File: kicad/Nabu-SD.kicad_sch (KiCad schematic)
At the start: 15 parts, among them J1 Nabu Expansion Slot, J2 ICSP, J3 SD Card, J4 Serial, J5 I2C, J6 OUT1, U1 PIC18F47Q84-E/P, U2 DS1307N+, Y1 32KHz

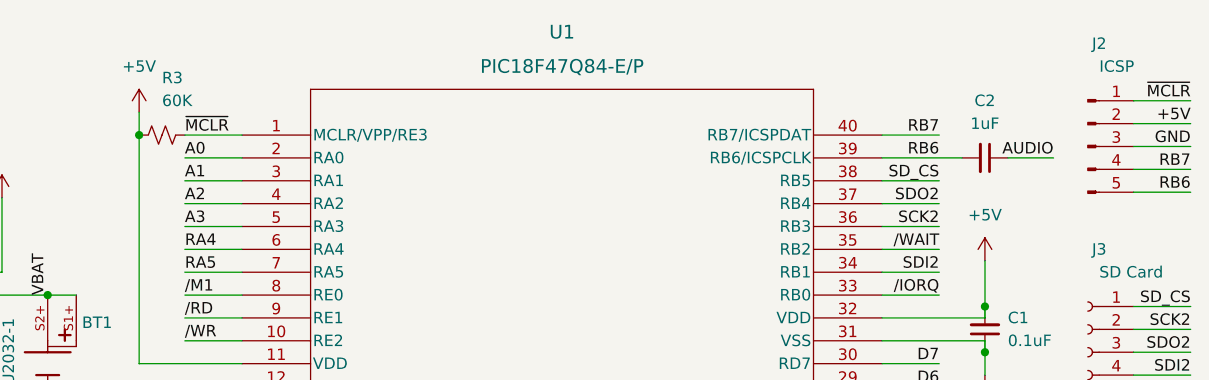
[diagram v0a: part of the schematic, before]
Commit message: Corrected 1 resistor value; Added a Solder Jumper to close AFTER flashing PIC. Reduced the size of the board.  Moved to mostly SMD parts (where possible).
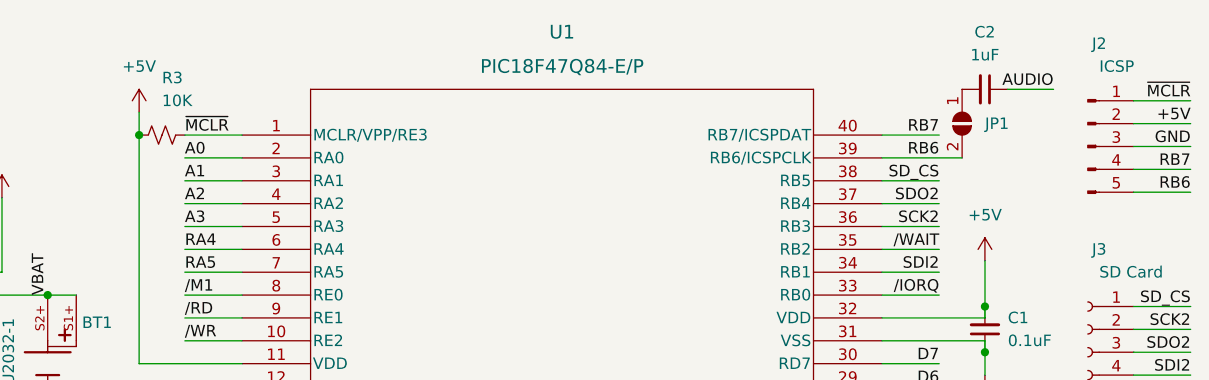
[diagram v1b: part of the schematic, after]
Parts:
- added JP1: ICSP Close, SolderJumper-2_P1.3mm_Open_TrianglePad1.0x1.5mm, symbol Jumper:SolderJumper_2_Open
- R3: value 60K -> 10K; Digi-Key_PN P60.4KCCT-ND -> P10.0KCCT-ND; LCSC C2077261 -> C169253; MPN ERJ-6ENF6042V -> ERJ-6ENF1002V
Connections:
- net RB6: now also JP1.2 (B); no longer C2.2
- new net: C2.2, JP1.1 (A)
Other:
- moved on the sheet: C2
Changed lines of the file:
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@@
+    (stroke (width 0) (type default) (color 0 0 0 0))
+  )
+  (wire (pts (xy 161.29 27.94) (xy 170.18 27.94))
     (stroke (width 0) (type default) (color 0 0 0 0))
   )
@@
     (stroke (width 0) (type default) (color 0 0 0 0))
   )
-  (wire (pts (xy 175.26 27.94) (xy 180.34 27.94))
+  (wire (pts (xy 175.26 20.32) (xy 180.34 20.32))
     (stroke (width 0) (type default) (color 0 0 0 0))
   )
@@
     (stroke (width 0) (type default) (color 0 0 0 0))
   )
-  (wire (pts (xy 161.29 27.94) (xy 170.18 27.94))
-    (stroke (width 0) (type default) (color 0 0 0 0))
-  )
   (wire (pts (xy 161.29 73.66) (xy 167.64 73.66))
     (stroke (width 0) (type default) (color 0 0 0 0))
@@
     (effects (font (size 1.27 1.27)) (justify right bottom))
   )
-  (label "AUDIO" (at 180.34 27.94 180)
+  (label "AUDIO" (at 180.34 20.32 180)
     (effects (font (size 1.27 1.27)) (justify right bottom))
   )
@@
       (effects (font (size 1.27 1.27)) (justify right))
     )
-    (property "Value" "60K" (id 1) (at 81.28 21.59 90)
+    (property "Value" "10K" (id 1) (at 81.28 21.59 90)
       (effects (font (size 1.27 1.27)) (justify right))
     )
@@
       (effects (font (size 1.27 1.27)) hide)
     )
-    (property "Description" "RES SMD 60.4K OHM 1% 1/8W 0805" (id 4) (at 81.28 25.4 0)
-      (effects (font (size 1.27 1.27)) hide)
-    )
-    (property "Digi-Key_PN" "P60.4KCCT-ND" (id 5) (at 81.28 25.4 0)
-      (effects (font (size 1.27 1.27)) hide)
-    )
-    (property "MPN" "ERJ-6ENF6042V" (id 6) (at 81.28 25.4 0)
+    (property "Description" "RES SMD 10K OHM 1% 1/8W 0805" (id 4) (at 81.28 25.4 0)
+      (effects (font (size 1.27 1.27)) hide)
+    )
+    (property "Digi-Key_PN" "P10.0KCCT-ND" (id 5) (at 81.28 25.4 0)
+      (effects (font (size 1.27 1.27)) hide)
+    )
+    (property "MPN" "ERJ-6ENF1002V" (id 6) (at 81.28 25.4 0)
       (effects (font (size 1.27 1.27)) hide)
     )
@@
       (effects (font (size 1.27 1.27)) hide)
     )
-    (property "LCSC" "C2077261" (id 8) (at 81.28 25.4 0)
+    (property "LCSC" "C169253" (id 8) (at 81.28 25.4 0)
       (effects (font (size 1.27 1.27)) hide)
     )
@@
     (pin "1")
   )
+  (symbol (lib_id "Jumper:SolderJumper_2_Open") (at 170.18 24.13 270) (unit 1)
+    (in_bom yes) (on_board yes) (fields_autoplaced)
+    (property "Reference" "JP1" (id 0) (at 172.72 24.1299 90)
+      (effects (font (size 1.27 1.27)) (justify left))
+    )
+    (property "Value" "ICSP Close" (id 1) (at 167.64 22.8601 90)
+      (effects (font (size 1.27 1.27)) (justify right) hide)
+    )
+    (property "Footprint" "SolderJumper-2_P1.3mm_Open_TrianglePad1.0x1.5mm" (id 2) (at 170.18 24.13 0)
+      (effects (font (size 1.27 1.27)) hide)
+    )
+    (property "Datasheet" "~" (id 3) (at 170.18 24.13 0)
+      (effects (font (size 1.27 1.27)) hide)
+    )
+    (pin "1")
+    (pin "2")
+  )
   (symbol (lib_id "Device:R_Small_US") (at 30.48 33.02 90) (unit 1)
     (in_bom yes) (on_board yes)
@@
     (pin "2")
   )
-  (symbol (lib_id "Device:C_Small") (at 172.72 27.94 270) (unit 1)
+  (symbol (lib_id "Device:C_Small") (at 172.72 20.32 270) (unit 1)
     (in_bom yes) (on_board yes) (fields_autoplaced)
-    (property "Reference" "C2" (id 0) (at 172.7136 21.59 90))
-    (property "Value" "1uF" (id 1) (at 172.7136 24.13 90))
-    (property "Footprint" "Capacitor_SMD:C_0805_2012Metric" (id 2) (at 172.72 27.94 0)
-      (effects (font (size 1.27 1.27)) hide)
-    )
-    (property "Datasheet" "https://media.digikey.com/pdf/Data%20Sheets/Samsung%20PDFs/CL21B105KBFNNNE_Spec.pdf" (id 3) (at 172.72 27.94 0)
-      (effects (font (size 1.27 1.27)) hide)
-    )
-    (property "Description" "CAP CER 1UF 50V X7R 0805" (id 4) (at 172.72 27.94 0)
-      (effects (font (size 1.27 1.27)) hide)
-    )
-    (property "Digi-Key_PN" "1276-1029-1-ND" (id 5) (at 172.72 27.94 0)
-      (effects (font (size 1.27 1.27)) hide)
-    )
-    (property "MPN" "CL21B105KBFNNNE" (id 6) (at 172.72 27.94 0)
-      (effects (font (size 1.27 1.27)) hide)
-    )
-    (property "Manufacturer" "Samsung Electro-Mechanics" (id 7) (at 172.72 27.94 0)
-      (effects (font (size 1.27 1.27)) hide)
-    )
-    (property "LCSC" "C28323" (id 8) (at 172.72 27.94 0)
+    (property "Reference" "C2" (id 0) (at 172.7136 13.97 90))
+    (property "Value" "1uF" (id 1) (at 172.7136 16.51 90))
+    (property "Footprint" "Capacitor_SMD:C_0805_2012Metric" (id 2) (at 172.72 20.32 0)
+      (effects (font (size 1.27 1.27)) hide)
+    )
+    (property "Datasheet" "https://media.digikey.com/pdf/Data%20Sheets/Samsung%20PDFs/CL21B105KBFNNNE_Spec.pdf" (id 3) (at 172.72 20.32 0)
+      (effects (font (size 1.27 1.27)) hide)
+    )
+    (property "Description" "CAP CER 1UF 50V X7R 0805" (id 4) (at 172.72 20.32 0)
+      (effects (font (size 1.27 1.27)) hide)
+    )
+    (property "Digi-Key_PN" "1276-1029-1-ND" (id 5) (at 172.72 20.32 0)
+      (effects (font (size 1.27 1.27)) hide)
+    )
+    (property "MPN" "CL21B105KBFNNNE" (id 6) (at 172.72 20.32 0)
+      (effects (font (size 1.27 1.27)) hide)
+    )
+    (property "Manufacturer" "Samsung Electro-Mechanics" (id 7) (at 172.72 20.32 0)
+      (effects (font (size 1.27 1.27)) hide)
+    )
+    (property "LCSC" "C28323" (id 8) (at 172.72 20.32 0)
       (effects (font (size 1.27 1.27)) hide)
     )
@@
       (reference "J6") (unit 1) (value "OUT1") (footprint "TestPoint:TestPoint_THTPad_D2.0mm_Drill1.0mm")
     )
+    (path "/967db7db-012b-4647-8660-62640790281e"
+      (reference "JP1") (unit 1) (value "ICSP Close") (footprint "SolderJumper-2_P1.3mm_Open_TrianglePad1.0x1.5mm")
+    )
     (path "/a2cfb6f2-23b4-4a08-8cc1-99aa0c54c5cb"
       (reference "R1") (unit 1) (value "10K") (footprint "Resistor_SMD:R_0805_2012Metric_Pad1.20x1.40mm_HandSolder")
@@
     )
     (path "/0677a4b0-9f16-4a73-9753-a478ee8d0e5a"
-      (reference "R3") (unit 1) (value "60K") (footprint "Resistor_SMD:R_0805_2012Metric_Pad1.20x1.40mm_HandSolder")
+      (reference "R3") (unit 1) (value "10K") (footprint "Resistor_SMD:R_0805_2012Metric_Pad1.20x1.40mm_HandSolder")
     )
     (path "/43fa6642-e48e-4ffc-8ec7-d314d3e03faf"

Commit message: Created the SD Card and Serial Card breakouts and included them in schematic. Prettied up all of the 3D Models and rendered them in the board view. Added all used external models, footprints, and symbols.
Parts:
- BT1: value BU2032-1 -> BU2032-1-HD-G; Digi-Key_PN BU2032-1-ND -> BU2032-1-HD-G-ND; MPN BU2032-1 -> BU2032-1-HD-G
- C1, C2: footprint Capacitor_SMD:C_0805_2012Metric -> Capacitor_SMD:C_0805_2012Metric_Pad1.18x1.45mm_HandSolder
- J1: Digi-Key_PN (none) -> 612-SSW-130-02-T-S-RA-ND; LCSC C2883747 -> (none); MPN (none) -> SSW-130-02-T-S-RA; Manufacturer (none) -> Samtec Inc.
- J2: Digi-Key_PN (none) -> 612-TSW-105-25-T-S-RA-ND; LCSC C2894947 -> C492413; MPN (none) -> TSW-105-25-T-S-RA; Manufacturer (none) -> Samtec Inc.
- J3, J4: Digi-Key_PN (none) -> SSW-106-02-TM-S-RA-ND; MPN (none) -> SSW-106-02-TM-S-RA; Manufacturer (none) -> Samtec Inc.
- J5: Digi-Key_PN (none) -> SAM15257-ND; MPN (none) -> SL-104-TT-19; Manufacturer (none) -> Samtec Inc.
- J6: Digi-Key_PN (none) -> SAM8859-ND; LCSC (none) -> C3715650; MPN (none) -> SNT-100-BK-G-H; Manufacturer (none) -> Samtec Inc.; now in the parts list
- JP1: value ICSP Close -> ICSP Disable; footprint SolderJumper-2_P1.3mm_Open_TrianglePad1.0x1.5mm -> Connector_PinHeader_2.54mm:PinHeader_1x02_P2.54mm_Horizontal; Digi-Key_PN (none) -> TSW-102-25-T-S-RA-ND; LCSC (none) -> C492410; MPN (none) -> TSW-102-25-T-S-RA; Manufacturer (none) -> Samtec Inc.
- U1: LCSC C3231788 -> C2874018
- Y1: footprint Nabu-SD:SMD3215-2P -> Nabu-SD:XTAL_ECS-.327-12.5-34B; Digi-Key_PN 3155-32.768K12.5P2/DT38-ND -> XC2294CT-ND; LCSC C5213671 -> (none); MPN 32.768K12.5P2/DT38 -> ECS-.327-12.5-34RR-TR; Manufacturer YIC -> ECS Inc.
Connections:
- net Serial_Breakout/+5V: now reaches J4.3 (Pin_3)
- net SCK2 renamed SPISCK
- net SDI2 renamed MISO
- net SDO2 renamed MOSI
- no-connect marks 1 -> 13
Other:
- added sheet MicroSD_Breakout (SD_Breakout.kicad_sch)
- added sheet Serial_Breakout (Serial_Breakout.kicad_sch)
- title: SD Card expansion for NABU -> SD Card Expansion & More! for NABU
- moved on the sheet: C1, C2, J1, J2, J3, J4, JP1, U1

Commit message: Updated LCSC part mappings. Updated LM1117-3.3 model and regenerated the PCB render.
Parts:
- U1: LCSC C2874018 -> C2684763; LCSC Part (none) -> C2874018
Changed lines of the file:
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@@
       (effects (font (size 1.27 1.27)) hide)
     )
-    (property "LCSC" "C2874018" (id 5) (at 65.405 22.86 0)
+    (property "LCSC" "C2684763" (id 5) (at 65.405 22.86 0)
       (effects (font (size 1.27 1.27)) hide)
     )
@@
       (effects (font (size 1.27 1.27)) hide)
     )
+    (property "LCSC Part" "C2874018" (id 12) (at 90.17 25.4 0)
+      (effects (font (size 1.27 1.27)) hide)
+    )

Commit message: Shuffled around PIC pins around for I2C and Serial CTS signals to be more inline with the datasheet for this specific PIC.
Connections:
- net SCL: now also U1.18 (RC3); no longer U1.17 (RC2)
- net SDA: now also U1.23 (RC4); no longer U1.18 (RC3)
- net RC4 renamed RC2
- net RC2: now also U1.17 (RC2); no longer U1.23 (RC4)
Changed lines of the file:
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@@
     (title "SD Card Expansion & More! for NABU")
     (date "2023-04-25")
-    (rev "1.0")
+    (rev "1.1")
   )
   (junction (at 146.05 44.45) (diameter 0) (color 0 0 0 0)
@@
     (effects (font (size 1.27 1.27)) (justify right bottom))
   )
-  (label "RC4" (at 140.97 68.58 180)
+  (label "SDA" (at 140.97 68.58 180)
     (effects (font (size 1.27 1.27)) (justify right bottom))
   )
@@
     (effects (font (size 1.27 1.27)) (justify right bottom))
   )
-  (label "RC4" (at 168.91 81.28 180)
+  (label "RC2" (at 168.91 81.28 180)
     (effects (font (size 1.27 1.27)) (justify right bottom))
   )
@@
     (effects (font (size 1.27 1.27)) (justify right bottom))
   )
-  (label "SCL" (at 83.82 66.04 0)
+  (label "RC2" (at 83.82 66.04 0)
     (effects (font (size 1.27 1.27)) (justify left bottom))
   )
@@
     (effects (font (size 1.27 1.27)) (justify right bottom))
   )
-  (label "SDA" (at 83.82 68.58 0)
-    (effects (font (size 1.27 1.27)) (justify left bottom))
-  )
+  (label "SCL" (at 83.82 68.58 0)
+    (effects (font (size 1.27 1.27)) (justify left bottom))
+  )

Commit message: Update +5V and +3V3 voltage trace widths per @K3130440 and greghol.
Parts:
- added C10: 10uF, Capacitor_SMD:C_0805_2012Metric_Pad1.18x1.45mm_HandSolder, symbol Device:C_Polarized_Small_US
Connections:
- net +5V: now also C10.1
- net GND: now also C10.2
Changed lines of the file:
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@@
   (junction (at 30.226 85.09) (diameter 0) (color 0 0 0 0)
+  )
+  (junction (at 27.686 85.09) (diameter 0) (color 0 0 0 0)
   )
   (junction (at 33.02 33.02) (diameter 0) (color 0 0 0 0)
@@
     (stroke (width 0) (type default) (color 0 0 0 0))
   )
-  (wire (pts (xy 27.686 102.87) (xy 27.686 85.09))
+  (wire (pts (xy 27.686 81.28) (xy 27.686 85.09))
     (stroke (width 0) (type default) (color 0 0 0 0))
   )
@@
     (stroke (width 0) (type default) (color 0 0 0 0))
   )
+  (wire (pts (xy 27.686 85.09) (xy 27.686 102.87))
+    (stroke (width 0) (type default) (color 0 0 0 0))
+  )
   (wire (pts (xy 146.05 48.26) (xy 146.05 49.53))
     (stroke (width 0) (type default) (color 0 0 0 0))
@@
   )
   (wire (pts (xy 75.946 102.87) (xy 75.946 93.98))
+    (stroke (width 0) (type default) (color 0 0 0 0))
+  )
+  (wire (pts (xy 22.606 81.28) (xy 22.606 85.09))
     (stroke (width 0) (type default) (color 0 0 0 0))
   )
@@
     )
     (pin "1")
+  )
+  (symbol (lib_id "Device:C_Polarized_Small_US") (at 25.146 81.28 270) (unit 1)
+    (in_bom yes) (on_board yes)
+    (property "Reference" "C10" (id 0) (at 26.416 74.93 0)
+      (effects (font (size 1.27 1.27)) (justify left))
+    )
+    (property "Value" "10uF" (id 1) (at 23.876 73.66 0)
+      (effects (font (size 1.27 1.27)) (justify left))
+    )
+    (property "Footprint" "Capacitor_SMD:C_0805_2012Metric_Pad1.18x1.45mm_HandSolder" (id 2) (at 25.146 81.28 0)
+      (effects (font (size 1.27 1.27)) hide)
+    )
+    (property "Datasheet" "https://media.digikey.com/pdf/Data%20Sheets/Samsung%20PDFs/CL_Series_MLCC_ds.pdf" (id 3) (at 25.146 81.28 0)
+      (effects (font (size 1.27 1.27)) hide)
+    )
+    (property "Description" "CAP CER 10UF 16V X7R 0805" (id 4) (at 25.146 81.28 0)
+      (effects (font (size 1.27 1.27)) hide)
+    )
+    (property "Digi-Key_PN" "1276-2872-1-ND" (id 5) (at 25.146 81.28 0)
+      (effects (font (size 1.27 1.27)) hide)
+    )
+    (property "MPN" "CL21B106KOQNNNE" (id 6) (at 25.146 81.28 0)
+      (effects (font (size 1.27 1.27)) hide)
+    )
+    (property "Manufacturer" "Samsung Electro-Mechanics" (id 7) (at 25.146 81.28 0)
+      (effects (font (size 1.27 1.27)) hide)
+    )
+    (property "LCSC" "C95841" (id 8) (at 26.3144 83.5914 0)
+      (effects (font (size 1.27 1.27)) hide)
+    )
+    (pin "1")
+    (pin "2")
   )
   (symbol (lib_id "power:+5V") (at 30.226 85.09 0) (mirror y) (unit 1)
@@
       (reference "C9") (unit 1) (value "0.1uF") (footprint "Capacitor_SMD:C_0805_2012Metric_Pad1.18x1.45mm_HandSolder")
     )
+    (path "/307e1165-bc81-4720-bca3-7717d7f64a78"
+      (reference "C10") (unit 1) (value "10uF") (footprint "Capacitor_SMD:C_0805_2012Metric_Pad1.18x1.45mm_HandSolder")
+    )
     (path "/2e0d8ec7-af9f-46be-8afa-5045d83789bd/0e87583a-57b2-4886-9be9-093b6ed25be5"

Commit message: Rotate Green LED 180 degrees on Serial breakout.
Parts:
- BT1: LCSC (none) -> C7091830
- J1: LCSC (none) -> C5909071
- Y1: LCSC (none) -> C2450273
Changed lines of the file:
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@@
       (effects (font (size 1.27 1.27)) hide)
     )
-    (property "LCSC" "~" (id 8) (at 45.72 26.67 0)
+    (property "LCSC" "C2450273" (id 8) (at 45.72 26.67 0)
       (effects (font (size 1.27 1.27)) hide)
     )
@@
       (effects (font (size 1.27 1.27)) hide)
     )
-    (property "LCSC" "~" (id 8) (at 68.58 50.8 0)
+    (property "LCSC" "C7091830" (id 8) (at 68.58 50.8 0)
       (effects (font (size 1.27 1.27)) hide)
     )
@@
       (effects (font (size 1.27 1.27)) hide)
     )
-    (property "LCSC" "~" (id 4) (at 53.086 107.95 0)
-      (effects (font (size 1.27 1.27)) hide)
-    )
+    (property "LCSC" "C5909071" (id 4) (at 53.086 107.95 0)
+      (effects (font (size 1.27 1.27)) hide)
+    )
